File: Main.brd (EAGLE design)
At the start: 100 x 80 mm, 27 parts, among them U1 L298, U2 LM 1085 IT5,0, U3 LM 1085 IT3,3, U4 L298, X1 12V

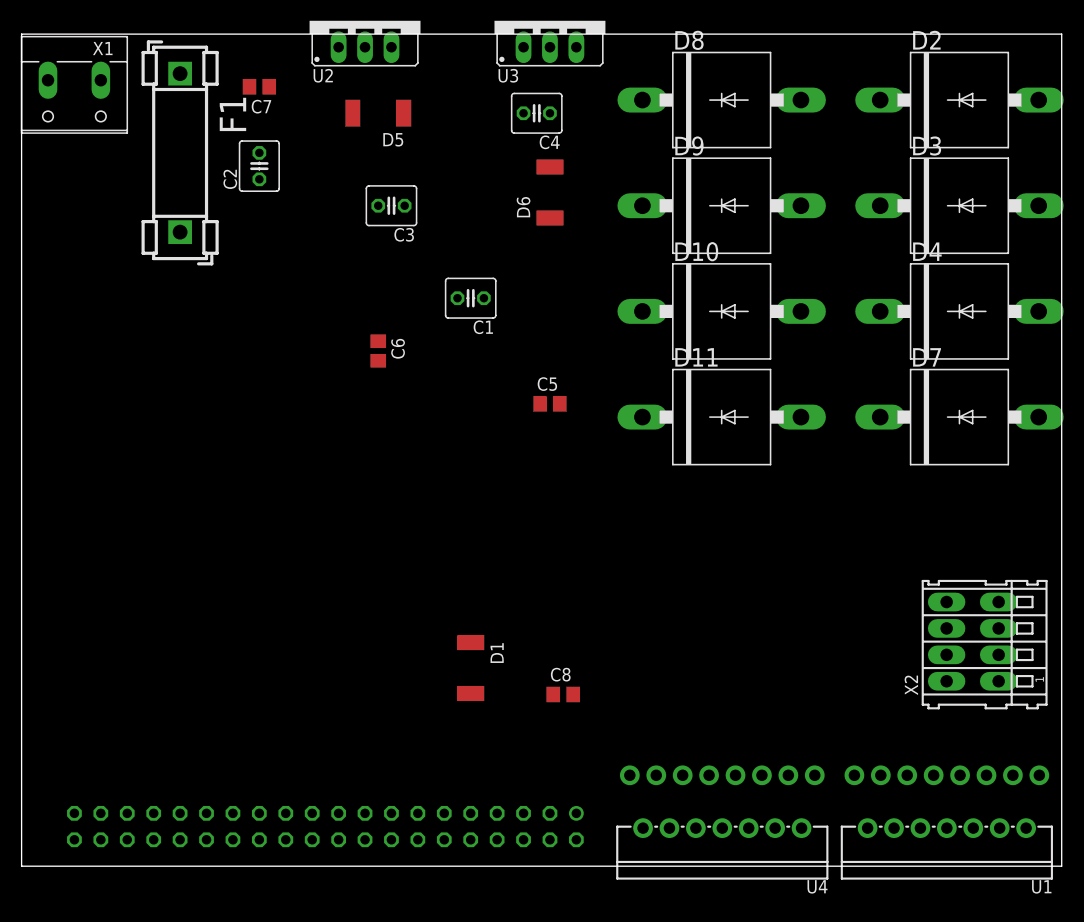
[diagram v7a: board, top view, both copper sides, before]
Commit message: using ria screw terminals
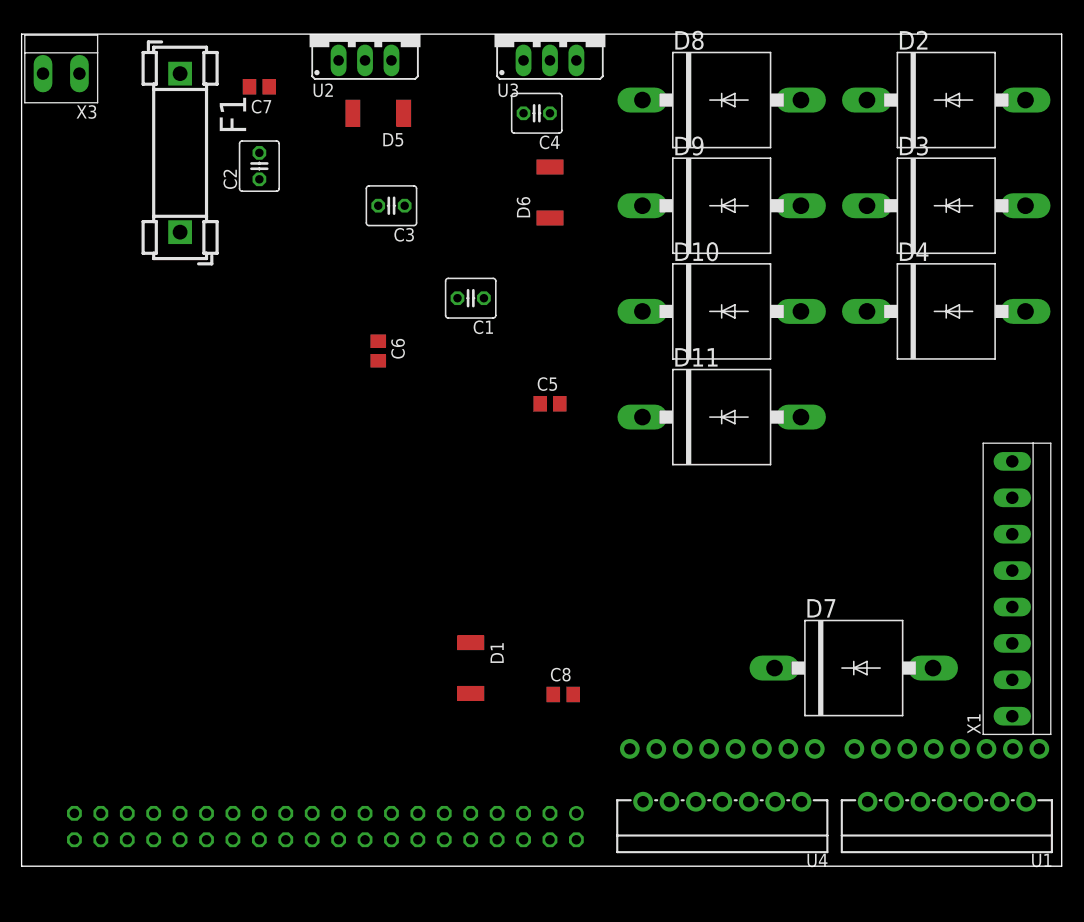
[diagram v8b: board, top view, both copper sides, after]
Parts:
- removed X2: (no value), con-wago255:233-504
- added X3: Battery, con-ria-59:2POL35
- SV1: value (none) -> Raspberry Pi B Plus Connector
- U2: value LM 1085 IT5,0 -> LM 1084 IT5,0; device linear-technology-3:TO220S -> v-reg-2:317TS
- U3: value LM 1085 IT3,3 -> LM 1084 IT3,3; device linear-technology-3:TO220S -> v-reg-2:317TS
- X1: value 12V -> Motors; device con-wago-508:W237-132 -> con-ria-59:8POL35
- moved X1 102.3 mm to (95.2, 26.7), turned to 90 degrees
- moved D7 26.2 mm to (80.0, 19.1)
- moved U1 2.54 mm to (88.9, 8.89)
- moved U4 2.54 mm to (67.3, 8.89)
- moved D2 1.27 mm to (88.9, 73.7)
- moved D3 1.27 mm to (88.9, 63.5)
- moved D4 1.27 mm to (88.9, 53.3)
- moved U2 1.27 mm to (33.0, 80.0)
- moved U3 1.27 mm to (50.8, 80.0)
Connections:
- net GND: now also X3.2; no longer X1.2
- net ML_OUT_A: now also X1.1, X1.3; no longer X2.A1
- net ML_OUT_B: now also X1.2, X1.4; no longer X2.A2
- net MR_OUT_A: now also X1.5, X1.7; no longer X2.A3
- net MR_OUT_B: now also X1.6, X1.8; no longer X2.A4
- net N$1: now also X3.1; no longer X1.1
